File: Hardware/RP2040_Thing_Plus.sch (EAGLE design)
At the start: 64 parts, among them J5 USB Female Type C Connector, J6 MICRO-SD-SDIOPUSH-PUSH, Q1 2.5A/30V, U1 MCP73831, U2 MAX17048, U3 AP2112K-3.3V, U4 W25QXX128MBIT, U5 RP2040, Y2 12MHz

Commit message: airwire corrections
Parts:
- removed C10: 2.2uF, SparkFun-Capacitors:2.2UF-0603-10V-20%
- removed C7: 1.0uF, SparkFun-Capacitors:1.0UF-0603-16V-10%-X7R
- removed R7: 10k, SparkFun-Resistors:10KOHM-0603-1/10W-1%
- removed R8: 330, SparkFun-Resistors:330OHM1/10W1%(0603)
- removed U1: MCP73831, SparkFun-PowerIC:MCP73831
- added C8: 1.0uF, SparkFun-Capacitors:1.0UF-0402T-16V-10%
- added C9: 2.2uF, SparkFun-Capacitors:2.2UF-0402_TIGHT-10V-10%-X5R
- added R1, R4: 5.1k, SparkFun-Resistors:5.1KOHM-0402T-1/16W-1%
- added R10, R17: 2.2k, SparkFun-Resistors:2.2KOHM-0402T-1/16W-1%
- added S1: MOMENTARY-SWITCH-SPST-SMD-5.2MM-TALL, SparkFun-Switches:MOMENTARY-SWITCH-SPST-SMD-5.2MM-TALL
- added U7: 3.3V, SparkFun-IC-Power:V_REG_AP2112K-3.3V
- J3: value (none) -> QWIIC_RIGHT_ANGLE
- J5: device SparkFun-Connectors:USB_C4-LAYER-ISOLATED -> SparkFun-Connectors:USB_C_4-LAYER-ISOLATED
- R15, R16: value 5.1k -> 10k; device SparkFun-Resistors:5.1KOHM5.1KOHM-0603-1/10W-1% -> SparkFun-Resistors:10KOHM-0402T-1/16W-1%
- R2: value 10k -> 1k; device SparkFun-Resistors:10KOHM-0603-1/10W-1% -> SparkFun-Resistors:1KOHM-0402T-1/16W-1%
- R3: value 1K -> 1k; device SparkFun-Resistors:1KOHM-1/10W-1%(0603) -> SparkFun-Resistors:1KOHM-0402T-1/16W-1%
- R5: value 2.2k -> 1k; device SparkFun-Resistors:2.2KOHM-0603-1/10W-1% -> SparkFun-Resistors:1KOHM-0402T-1/16W-1%
- R9: value 2.2k -> 10k; device SparkFun-Resistors:2.2KOHM-0603-1/10W-1% -> SparkFun-Resistors:10KOHM-0402T-1/16W-1%
- U3: value AP2112K-3.3V -> MCP73831; device SparkFun-PowerIC:V_REG_LDOSMD -> SparkFun-IC-Power:MCP73831; PROD_ID VREG-12457 -> (none)
- renumbered U$3 to U6
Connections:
- removed net D13: D4.A
- removed net VIN: C7.1, D2.C, Q1.S, R2.2, U3.IN
- new net BOOT: R5.2, S1.2
- new net N$15: C8.1, D2.C, Q1.S, R16.2, U7.IN
- net 3.3V: now also C9.1, R9.2, U7.OUT; no longer C10.1, U3.OUT
- net EN: now also R16.1, U7.EN; no longer R2.1, U3.EN
- net GND: now also C8.2, C9.2, R1.2, R15.1, R3.1, R4.2, S1.1, U3.VSS, U7.GND; no longer C10.2, C7.2, R15.2, R16.2, R7.1, R8.1, U1.VSS, U3.GND
- net I2C1_SCL: now also R10.1; no longer R5.1
- net I2C1_SDA: now also R17.1; no longer R9.1
- net LED_BUILTIN: now also D4.A
- net N$1: now also R3.2; no longer R8.2
- net N$11: now also R1.1; no longer R15.1
- net N$12: now also R4.1; no longer R16.1
- net N$14: now also U3.PROG; no longer U1.PROG
- net N$17: now also R2.1; no longer R3.2
- net N$2: now also R10.2; no longer R5.2
- net N$3: now also R17.2; no longer R9.2
- net N$9: now also U3.STAT; no longer U1.STAT
- net QSPI-CS: now also R5.1, R9.1
- net V_BATT: now also U3.VBAT; no longer U1.VBAT
- net V_USB: now also R15.2, R2.2, U3.VIN; no longer R3.1, R7.2, U1.VIN
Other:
- note added: "BLINK LED"
- note added: "Boot Select"
- note removed: "GPIO13 LED"
- moved on the sheet: D2, D4, Q1, R2, R3, R5, R9, S2

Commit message: v01 review
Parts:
- removed C19, C6: 4.7uF, SparkFun-Capacitors:4.7UF-0603-6.3V-(10%)
- removed R14: 200, SparkFun-Resistors:200OHM-0603-1/10W-1%
- added C10, C7: 4.7uF, SparkFun-Capacitors:4.7UF-0402_TIGHT-6.3V-20%-X5R
- added J1: CORTEX_JTAG_DEBUG_MINIMUM_PTH, SparkFun-Connectors:CORTEX_JTAG_DEBUG_MINIMUM_PTH
- added R7: 200OHM-0402T-1/16W-1%, SparkFun-Resistors:200OHM-0402T-1/16W-1%
- R6: value 2.0k -> 2.0KOHM-0402T-1/16W-5%; device SparkFun-Resistors:2.0KOHM1/10W5%(0603) -> SparkFun-Resistors:2.0KOHM-0402T-1/16W-5%
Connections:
- net N$7 renamed USB_F_N
- net N$8 renamed USB_F_P
- removed net D+: J5.D+
- removed net D-: J5.D-
- removed net I2C1_SCL: J3.4, J8.11, R10.1, U2.SCL, U5.GPIO7
- removed net N$10: C28.1, R14.1, U5.ADC_VDD
- removed net N$23: U5.GPIO8
- removed net USB_D+: R13.1
- removed net USB_D-: R12.1
- new net AVDD: C28.1, J7.3, R7.1, U5.ADC_VDD
- new net I2C1_SCL/GPIO23: J3.4, J8.11, R10.1, U2.SCL, U5.GPIO23, U5.GPIO7
- new net USB_N: J5.D-, R12.1
- new net USB_P: J5.D+, R13.1
- net !RESET: now also J1.!RESET
- net 3.3V: now also J1.VCC, R7.2; no longer R14.2
- net BATT_ALERT: now also U5.GPIO24; no longer U5.GPIO5
- net GND: now also C10.2, C7.2, J1.GND; no longer C19.2, C6.2
- net GPIO16: now also J8.4; no longer J8.10
- net GPIO17: now also J8.5; no longer J8.9
- net GPIO18: now also J8.6; no longer J8.8
- net GPIO20: now also J8.8; no longer J8.6
- net GPIO21: now also J8.9; no longer J8.5
- net GPIO22: now also J8.10; no longer J8.4
- net N$13: now also U5.GPIO5; no longer U5.GPIO23
- net SWDCK: now also J1.SWDCLK
- net SWDIO: now also J1.SWDIO
- net V_BATT: now also C10.1; no longer C6.1
- net V_USB: now also C7.1; no longer C19.1
- net WS2812_DI: now also U5.GPIO8; no longer U5.GPIO24
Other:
- note added: "Debug Header"
- moved on the sheet: C8, C9, D1, D2, J4, Q1, R15, R16, R2, R6, U3, U7

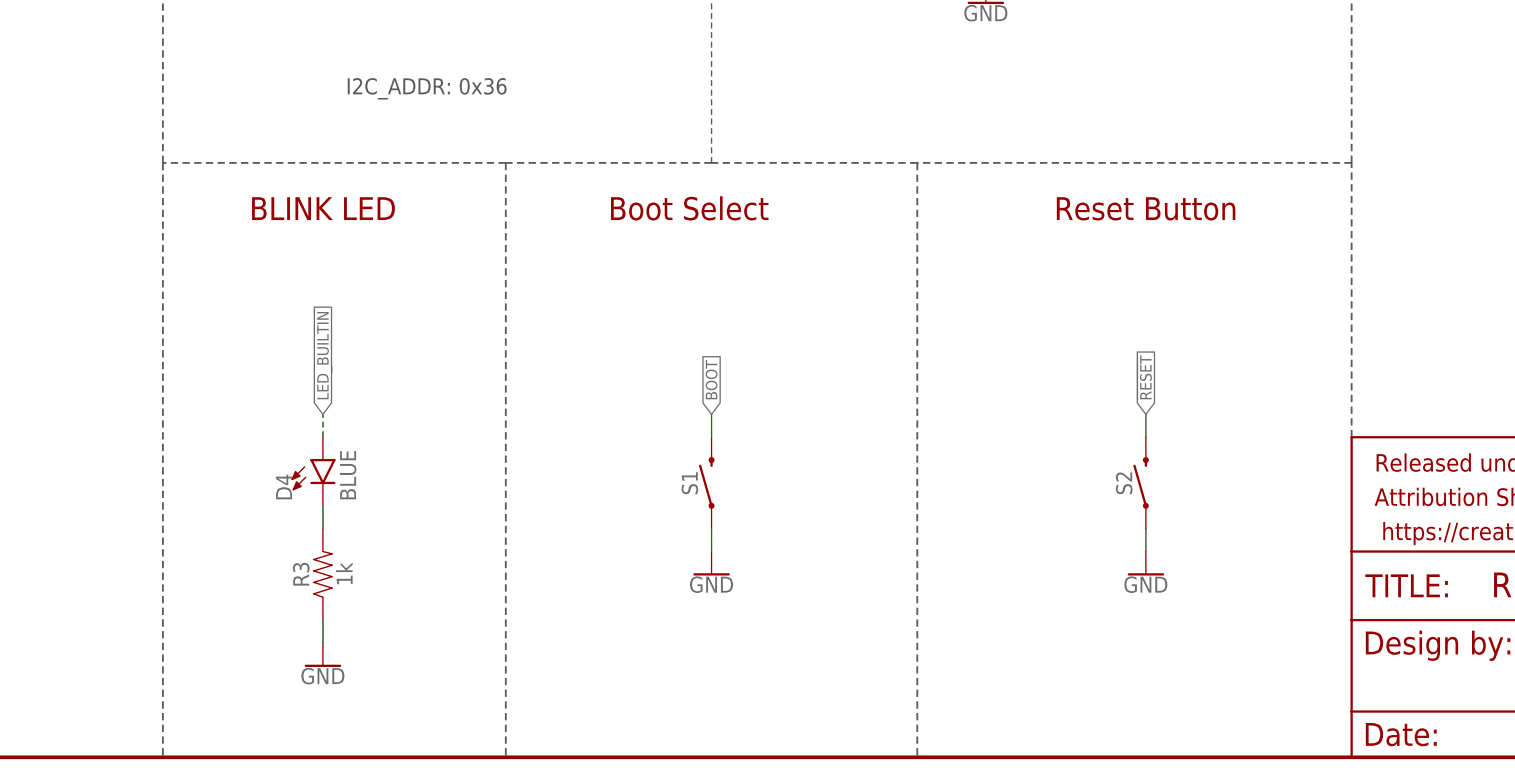
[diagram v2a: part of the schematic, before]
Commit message: Review Changes
- Add "Pi Thing Plus RP2040" silk
- Align LEDs
- Change LED label style
- Flip bottom silk labels
- Add GND vias
- Beef up power traces
- Add thermal vias under RP2040
- Straighten trace on ADC0
- Add SDA/SCL Labels to bottom silk
- Add PWR LED
- Move QSPI resistors to make room for silk

Passes micromod.dru (overlap errors for jumper footprint + thermal vias)
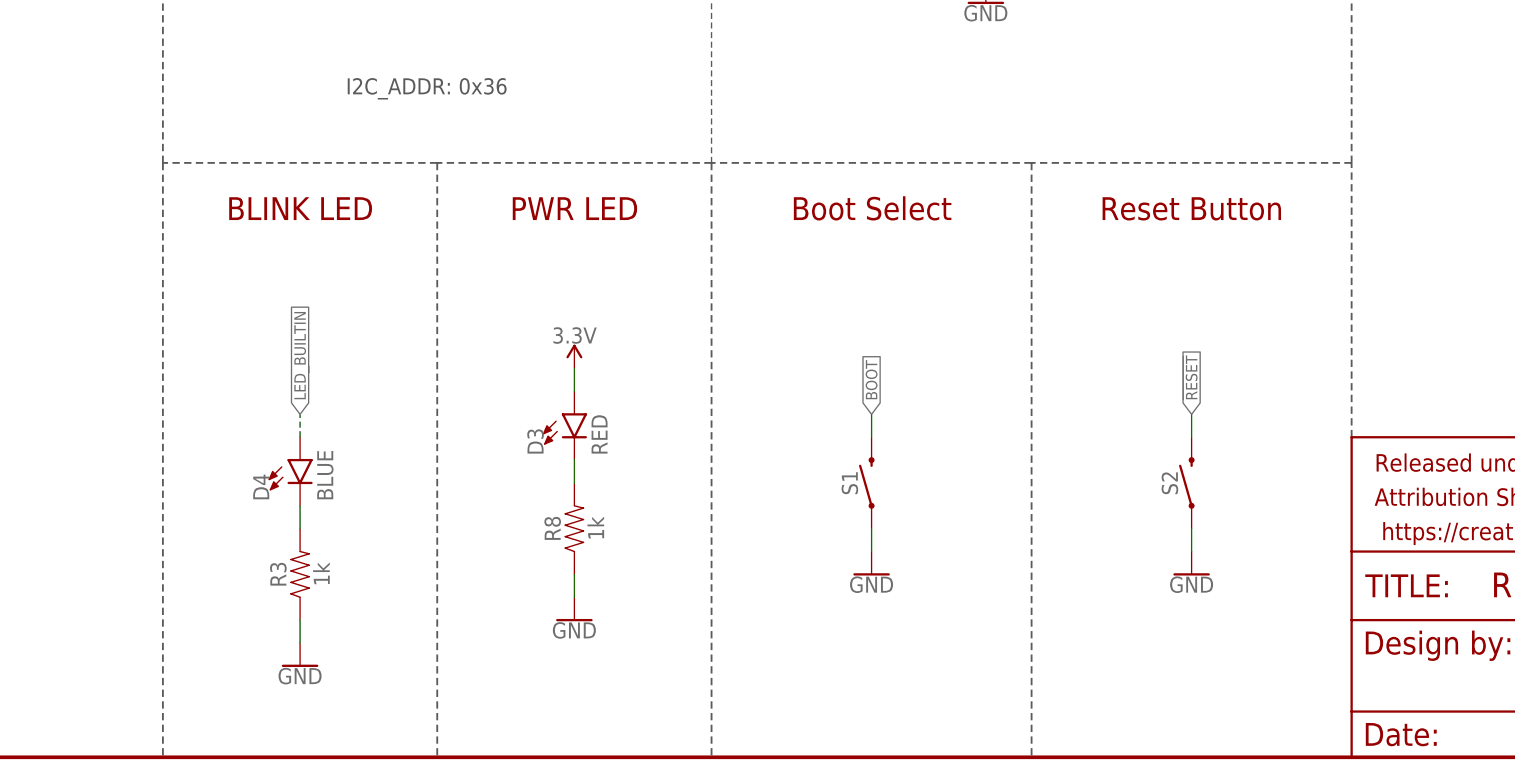
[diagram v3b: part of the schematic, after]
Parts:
- added D3: RED, SparkFun-LED:LED-RED0603
- added R8: 1k, SparkFun-Resistors:1KOHM-0402T-1/16W-1%
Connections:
- new net N$7: D3.C, R8.2
- net 3.3V: now also D3.A
- net GND: now also R8.1
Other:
- note added: "PWR LED"
- moved on the sheet: D4, R3, S1, S2

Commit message: Run lib update on schematic. Compress schematic wires. Push production files.
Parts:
- J1: value CORTEX_JTAG_DEBUG_MINIMUM_PTH -> SWD
- J3: value QWIIC_RIGHT_ANGLE -> Qwiic
- J5: value USB Female Type C Connector -> USB C
- J6: value MICRO-SD-SDIOPUSH-PUSH -> microSD
- Q1: value 2.5A/30V -> 20V/4.2A/52mΩ/1.4W; device SparkFun-DiscreteSemi:MOSFET-PCHANNELDMG2307L -> SparkFun-DiscreteSemi:MOSFET_PCH-DMG2305UX-7
- R6: value 2.0KOHM-0402T-1/16W-5% -> 1k; device SparkFun-Resistors:2.0KOHM-0402T-1/16W-5% -> SparkFun-Resistors:1KOHM-0402T-1/16W-1%
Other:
- note added: "16MB / 128mbit Flash"
- note added: "Power LED"
- note added: "Qwiic Connector"
- note added: "Status LED"
- note removed: "BLINK LED"
- note removed: "Flash"
- note removed: "PWR LED"
- note removed: "QWIIC Connector"
- moved on the sheet: C1, C10, C7, C9, J4, R1, R15, R4, R6, U2

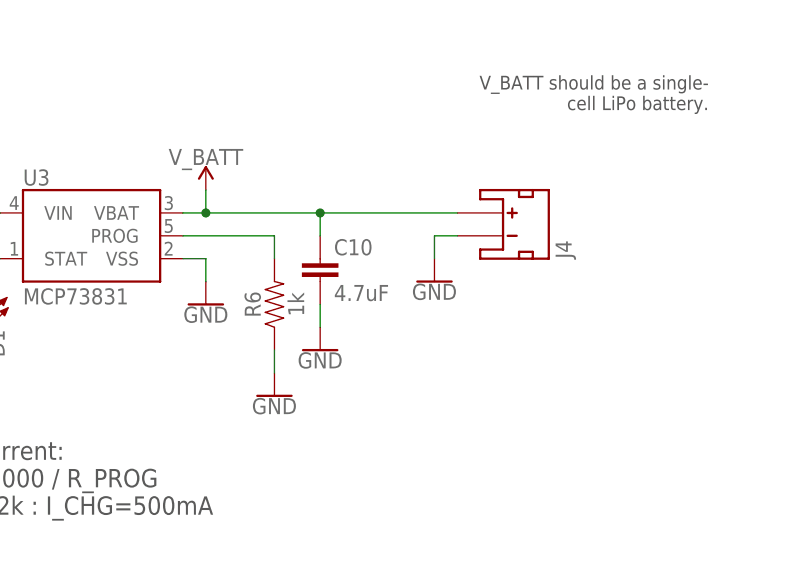
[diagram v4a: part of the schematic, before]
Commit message: Change res on charger to 2k
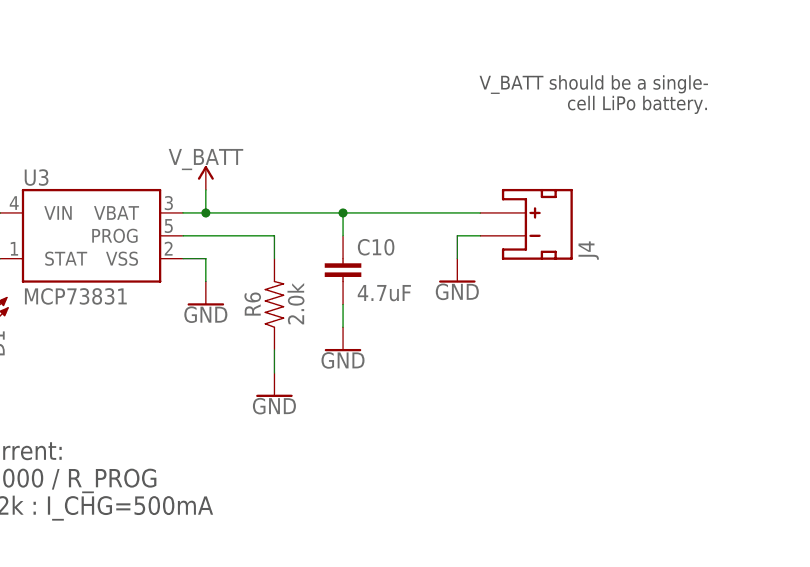
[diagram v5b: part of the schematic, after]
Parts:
- R6: value 1k -> 2.0k; device SparkFun-Resistors:1KOHM-0402T-1/16W-1% -> SparkFun-Resistors:2.0KOHM-0603-1/10W-5%
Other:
- moved on the sheet: C10, J4

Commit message: Panel with 2k charge resistor
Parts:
- removed LOGO1: FOUR_LAYER_WARNING, SparkFun-Aesthetics:FOUR_LAYER_WARNING
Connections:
- net SDIO_DAT1/AUD_IN renamed SDIO_DAT1
- net SDIO_DAT2/AUD_OUT renamed SDIO_DAT2
- removed net N$13: U5.GPIO5
- removed net N$24: U5.GPIO13
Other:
- note added: "Cut the I2C pullup jumper to remove the pullups from the SDA and SCL lines"
- note removed: "Disconnect the I2C Pullup jumper to remove the pullups from the SDA and SCL lines"

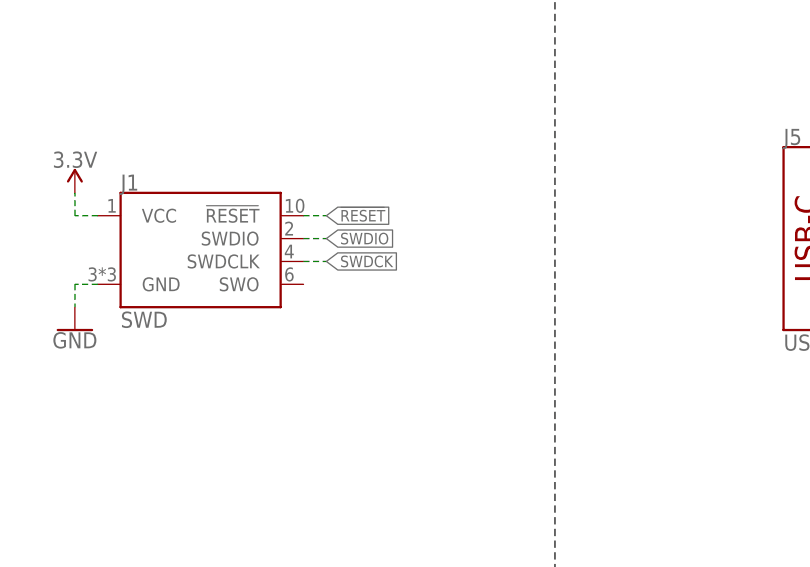
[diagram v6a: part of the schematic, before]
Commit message: Add TPs to SWD. Connect reset. v11.
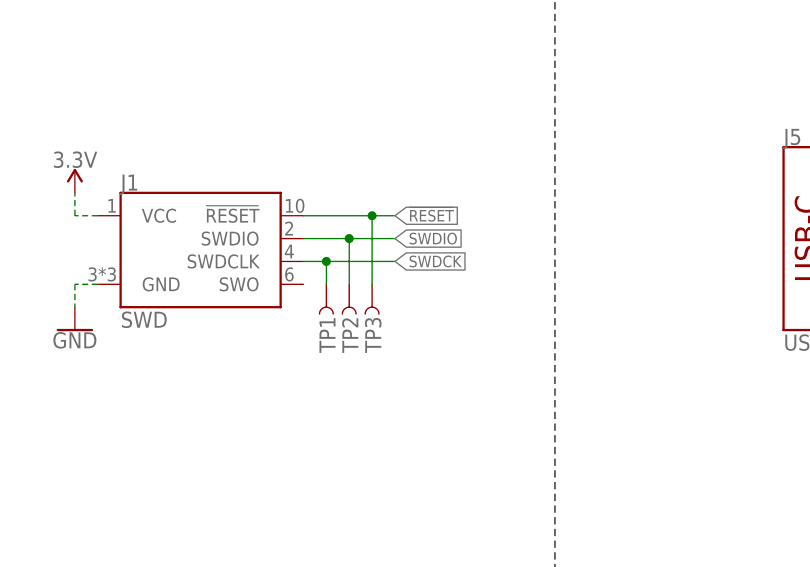
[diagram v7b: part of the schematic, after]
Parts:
- added TP1, TP2, TP3: TEST-POINT3X4, SparkFun-Connectors:TEST-POINT3X4
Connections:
- removed net !RESET: J1.!RESET, J7.1, S2.2
- net !RESET!: now also J1.!RESET, J7.1, S2.2, TP3.1
- net SWDCK: now also TP1.1
- net SWDIO: now also TP2.1
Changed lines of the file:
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@@
 <part name="SUPPLY36" library="SparkFun-PowerSymbols" deviceset="3.3V" device=""/>
 <part name="GND42" library="SparkFun-PowerSymbols" deviceset="GND" device=""/>
+<part name="TP1" library="SparkFun-Connectors" deviceset="TEST-POINT" device="3X4" value=""/>
+<part name="TP2" library="SparkFun-Connectors" deviceset="TEST-POINT" device="3X4" value=""/>
+<part name="TP3" library="SparkFun-Connectors" deviceset="TEST-POINT" device="3X4" value=""/>
 </parts>
 <sheets>
@@
 <attribute name="VALUE" x="386.08" y="215.646" size="1.778" layer="96" align="top-center"/>
 </instance>
+<instance part="TP1" gate="G$1" x="304.8" y="231.14" smashed="yes" rot="R270">
+<attribute name="NAME" x="304.038" y="227.584" size="1.778" layer="95" font="vector" rot="R270"/>
+<attribute name="VALUE" x="302.26" y="233.68" size="1.778" layer="96" font="vector" rot="R270"/>
+</instance>
+<instance part="TP2" gate="G$1" x="307.34" y="231.14" smashed="yes" rot="R270">
+<attribute name="NAME" x="306.578" y="227.584" size="1.778" layer="95" font="vector" rot="R270"/>
+<attribute name="VALUE" x="304.8" y="233.68" size="1.778" layer="96" font="vector" rot="R270"/>
+</instance>
+<instance part="TP3" gate="G$1" x="309.88" y="231.14" smashed="yes" rot="R270">
+<attribute name="NAME" x="309.118" y="227.584" size="1.778" layer="95" font="vector" rot="R270"/>
+<attribute name="VALUE" x="307.34" y="233.68" size="1.778" layer="96" font="vector" rot="R270"/>
+</instance>
 </instances>
 <busses>
@@
 <segment>
 <pinref part="J1" gate="G$1" pin="SWDIO"/>
-<wire x1="302.26" y1="236.22" x2="304.8" y2="236.22" width="0.1524" layer="91" style="longdash"/>
-<label x="304.8" y="236.22" size="1.27" layer="95" xref="yes"/>
-</segment>
-</net>
-<net name="!RESET" class="0">
-<segment>
-<wire x1="391.16" y1="88.9" x2="393.7" y2="88.9" width="0.1524" layer="91"/>
-<label x="393.7" y="88.9" size="1.27" layer="95" font="vector" xref="yes"/>
-<pinref part="J7" gate="G$1" pin="1"/>
-</segment>
-<segment>
-<wire x1="312.42" y1="35.56" x2="312.42" y2="38.1" width="0.1524" layer="91"/>
-<label x="312.42" y="38.1" size="1.27" layer="95" font="vector" rot="R90" xref="yes"/>
-<pinref part="S2" gate="G$1" pin="2"/>
-</segment>
-<segment>
-<pinref part="J1" gate="G$1" pin="!RESET"/>
-<wire x1="302.26" y1="238.76" x2="304.8" y2="238.76" width="0.1524" layer="91" style="longdash"/>
-<label x="304.8" y="238.76" size="1.27" layer="95" xref="yes"/>
+<wire x1="302.26" y1="236.22" x2="307.34" y2="236.22" width="0.1524" layer="91"/>
+<label x="312.42" y="236.22" size="1.27" layer="95" xref="yes"/>
+<pinref part="TP2" gate="G$1" pin="1"/>
+<wire x1="307.34" y1="236.22" x2="312.42" y2="236.22" width="0.1524" layer="91"/>
+<wire x1="307.34" y1="231.14" x2="307.34" y2="236.22" width="0.1524" layer="91"/>
+<junction x="307.34" y="236.22"/>
 </segment>
 </net>
@@
 <pinref part="U5" gate="U1" pin="RUN"/>
 </segment>
+<segment>
+<wire x1="391.16" y1="88.9" x2="393.7" y2="88.9" width="0.1524" layer="91"/>
+<label x="393.7" y="88.9" size="1.27" layer="95" font="vector" xref="yes"/>
+<pinref part="J7" gate="G$1" pin="1"/>
+</segment>
+<segment>
+<wire x1="312.42" y1="35.56" x2="312.42" y2="38.1" width="0.1524" layer="91"/>
+<label x="312.42" y="38.1" size="1.27" layer="95" font="vector" rot="R90" xref="yes"/>
+<pinref part="S2" gate="G$1" pin="2"/>
+</segment>
+<segment>
+<pinref part="J1" gate="G$1" pin="!RESET"/>
+<wire x1="302.26" y1="238.76" x2="309.88" y2="238.76" width="0.1524" layer="91"/>
+<label x="312.42" y="238.76" size="1.27" layer="95" xref="yes"/>
+<pinref part="TP3" gate="G$1" pin="1"/>
+<wire x1="309.88" y1="238.76" x2="312.42" y2="238.76" width="0.1524" layer="91"/>
+<wire x1="309.88" y1="231.14" x2="309.88" y2="238.76" width="0.1524" layer="91"/>
+<junction x="309.88" y="238.76"/>
+</segment>
 </net>
 <net name="SWDCK" class="0">
@@
 <segment>
 <pinref part="J1" gate="G$1" pin="SWDCLK"/>
-<wire x1="302.26" y1="233.68" x2="304.8" y2="233.68" width="0.1524" layer="91" style="longdash"/>
-<label x="304.8" y="233.68" size="1.27" layer="95" xref="yes"/>
-</segment>
-</net>
+<wire x1="302.26" y1="233.68" x2="304.8" y2="233.68" width="0.1524" layer="91"/>
+<label x="312.42" y="233.68" size="1.27" layer="95" xref="yes"/>
+<pinref part="TP1" gate="G$1" pin="1"/>
+<wire x1="304.8" y1="233.68" x2="312.42" y2="233.68" width="0.1524" layer="91"/>
+<wire x1="304.8" y1="231.14" x2="304.8" y2="233.68" width="0.1524" layer="91"/>
+<junction x="304.8" y="233.68"/>
+</segment>
+</net>
